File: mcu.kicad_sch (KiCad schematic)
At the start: 28 parts, among them J13 Conn_ARM_JTAG_SWD_10, J3 Conn_01x09_Socket, SW1 SW_SPST, U10 WE-TVS-824015043, U6 STM32F469VETx, Y2 8MHz

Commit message: Some fixes
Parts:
- added C25, C26: .1uF, Capacitor_SMD:C_0805_2012Metric, symbol Device:C
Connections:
- net +3.3V: now also C25.1, C26.1
- net GND: now also C25.2, C26.2
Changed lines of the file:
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@@
 	)
 	(junction
+		(at 139.7 256.54)
+		(diameter 0)
+		(color 0 0 0 0)
+	)
+	(junction
 		(at 185.42 224.79)
 		(diameter 0)
@@
 	)
 	(junction
+		(at 162.56 256.54)
+		(diameter 0)
+		(color 0 0 0 0)
+	)
+	(junction
 		(at 200.66 256.54)
 		(diameter 0)
@@
 	)
 	(junction
+		(at 139.7 224.79)
+		(diameter 0)
+		(color 0 0 0 0)
+	)
+	(junction
 		(at 25.4 72.39)
 		(diameter 0)
@@
 	)
 	(junction
+		(at 162.56 224.79)
+		(diameter 0)
+		(color 0 0 0 0)
+	)
+	(junction
 		(at 215.9 256.54)
 		(diameter 0)
@@
 	(wire
 		(pts
+			(xy 139.7 224.79) (xy 133.35 224.79)
+		)
+		(stroke
+			(width 0)
+			(type default)
+		)
+	)
+	(wire
+		(pts
 			(xy 193.04 234.95) (xy 193.04 224.79)
 		)
@@
 	(wire
 		(pts
+			(xy 162.56 224.79) (xy 170.18 224.79)
+		)
+		(stroke
+			(width 0)
+			(type default)
+		)
+	)
+	(wire
+		(pts
 			(xy 25.4 85.09) (xy 41.91 85.09)
 		)
@@
 	(wire
 		(pts
-			(xy 154.94 224.79) (xy 170.18 224.79)
+			(xy 154.94 224.79) (xy 162.56 224.79)
 		)
 		(stroke
@@
 	(wire
 		(pts
-			(xy 154.94 256.54) (xy 170.18 256.54)
+			(xy 154.94 256.54) (xy 162.56 256.54)
 		)
 		(stroke
@@
 	(wire
 		(pts
+			(xy 133.35 242.57) (xy 133.35 256.54)
+		)
+		(stroke
+			(width 0)
+			(type default)
+		)
+	)
+	(wire
+		(pts
 			(xy 91.44 242.57) (xy 92.71 242.57)
 		)
@@
 	(wire
 		(pts
+			(xy 162.56 256.54) (xy 170.18 256.54)
+		)
+		(stroke
+			(width 0)
+			(type default)
+		)
+	)
+	(wire
+		(pts
 			(xy 50.8 163.83) (xy 60.96 163.83)
 		)
@@
 	(wire
 		(pts
+			(xy 133.35 256.54) (xy 139.7 256.54)
+		)
+		(stroke
+			(width 0)
+			(type default)
+		)
+	)
+	(wire
+		(pts
 			(xy 91.44 232.41) (xy 109.22 232.41)
 		)
@@
 	(wire
 		(pts
+			(xy 162.56 224.79) (xy 162.56 234.95)
+		)
+		(stroke
+			(width 0)
+			(type default)
+		)
+	)
+	(wire
+		(pts
 			(xy 223.52 242.57) (xy 223.52 256.54)
 		)
@@
 	(wire
 		(pts
+			(xy 162.56 242.57) (xy 162.56 256.54)
+		)
+		(stroke
+			(width 0)
+			(type default)
+		)
+	)
+	(wire
+		(pts
 			(xy 25.4 67.31) (xy 41.91 67.31)
 		)
@@
 	(wire
 		(pts
+			(xy 133.35 224.79) (xy 133.35 234.95)
+		)
+		(stroke
+			(width 0)
+			(type default)
+		)
+	)
+	(wire
+		(pts
 			(xy 177.8 224.79) (xy 185.42 224.79)
 		)
@@
 	(symbol
 		(lib_id "Device:C")
+		(at 133.35 238.76 0)
+		(unit 1)
+		(exclude_from_sim no)
+		(in_bom yes)
+		(on_board yes)
+		(dnp no)
+		(property "Reference" "C26"
+			(at 135.382 235.966 0)
+			(effects
+				(font
+					(size 1.27 1.27)
+				)
+				(justify left)
+			)
+		)
+		(property "Value" ".1uF"
+			(at 135.382 241.554 0)
+			(effects
+				(font
+					(size 1.27 1.27)
+				)
+				(justify left)
+			)
+		)
+		(property "Footprint" "Capacitor_SMD:C_0805_2012Metric"
+			(at 134.3152 242.57 0)
+			(effects
+				(font
+					(size 1.27 1.27)
+				)
+				(hide yes)
+			)
+		)
+		(property "Datasheet" "~"
+			(at 133.35 238.76 0)
+			(effects
+				(font
+					(size 1.27 1.27)
+				)
+				(hide yes)
+			)
+		)
+		(property "Description" "Unpolarized capacitor"
+			(at 133.35 238.76 0)
+			(effects
+				(font
+					(size 1.27 1.27)
+				)
+				(hide yes)
+			)
+		)
+		(pin "2"
+		)
+		(pin "1"
+		)
+		(instances
+			(project "senior_design"
+				(path "/35c074f0-8545-4dc1-a57d-3ef0bc7d9188/332aa9c6-46d1-4f07-ac6a-0c48b9b46fa2"
+					(reference "C26")
+					(unit 1)
+				)
+			)
+		)
+	)
+	(symbol
+		(lib_id "Device:C")
 		(at 215.9 238.76 0)
 		(unit 1)
@@
 					(unit 1)
 				)
+			)
+		)
+	)
+	(symbol
+		(lib_id "Device:C")
+		(at 162.56 238.76 0)
+		(unit 1)
+		(exclude_from_sim no)
+		(in_bom yes)
+		(on_board yes)
+		(dnp no)
+		(property "Reference" "C25"
+			(at 164.592 235.966 0)
+			(effects
+				(font
+					(size 1.27 1.27)
+				)
+				(justify left)
+			)
+		)
+		(property "Value" ".1uF"
+			(at 164.592 241.554 0)
+			(effects
+				(font
+					(size 1.27 1.27)
+				)
+				(justify left)
+			)
+		)
+		(property "Footprint" "Capacitor_SMD:C_0805_2012Metric"
+			(at 163.5252 242.57 0)
+			(effects
+				(font
+					(size 1.27 1.27)
+				)
+				(hide yes)
+			)
+		)
+		(property "Datasheet" "~"
+			(at 162.56 238.76 0)
+			(effects
+				(font
+					(size 1.27 1.27)
+				)
+				(hide yes)
+			)
+		)
+		(property "Description" "Unpolarized capacitor"
+			(at 162.56 238.76 0)
+			(effects
+				(font
+					(size 1.27 1.27)
+				)
+				(hide yes)
+			)
+		)
+		(pin "2"
+		)
+		(pin "1"
+		)
+		(instances
+			(project "senior_design"
+				(path "/35c074f0-8545-4dc1-a57d-3ef0bc7d9188/332aa9c6-46d1-4f07-ac6a-0c48b9b46fa2"
+					(reference "C25")
+					(unit 1)
+				)

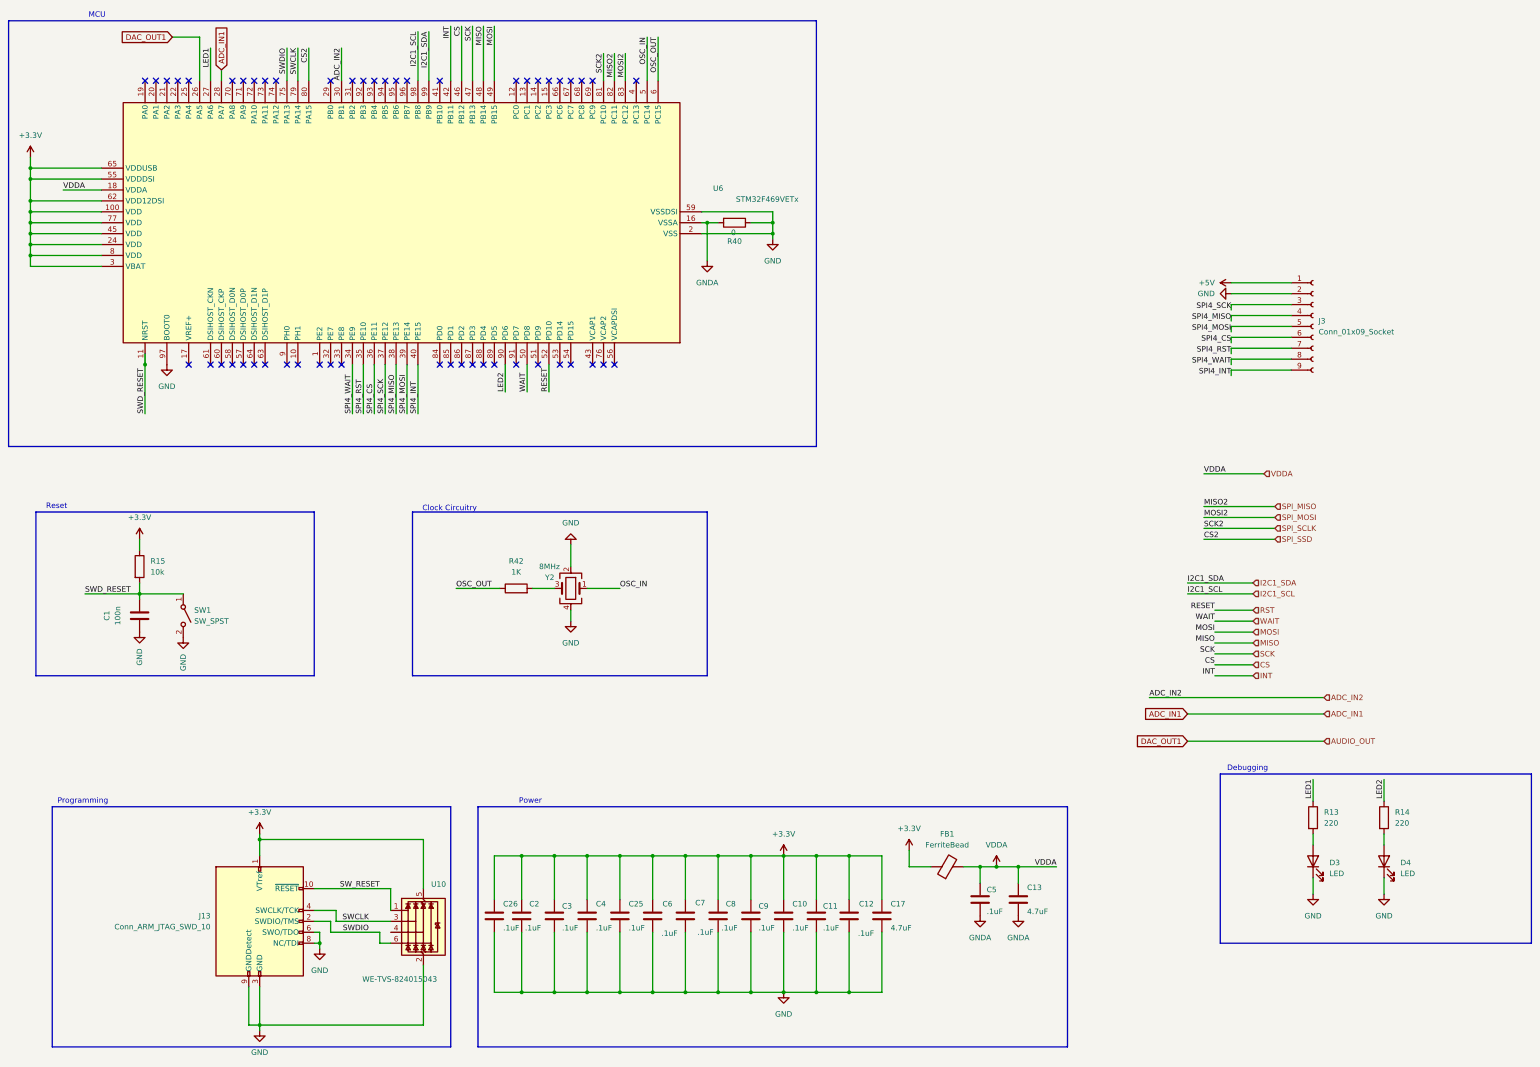
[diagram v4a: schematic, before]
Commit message: Fixed labels and added datasheets
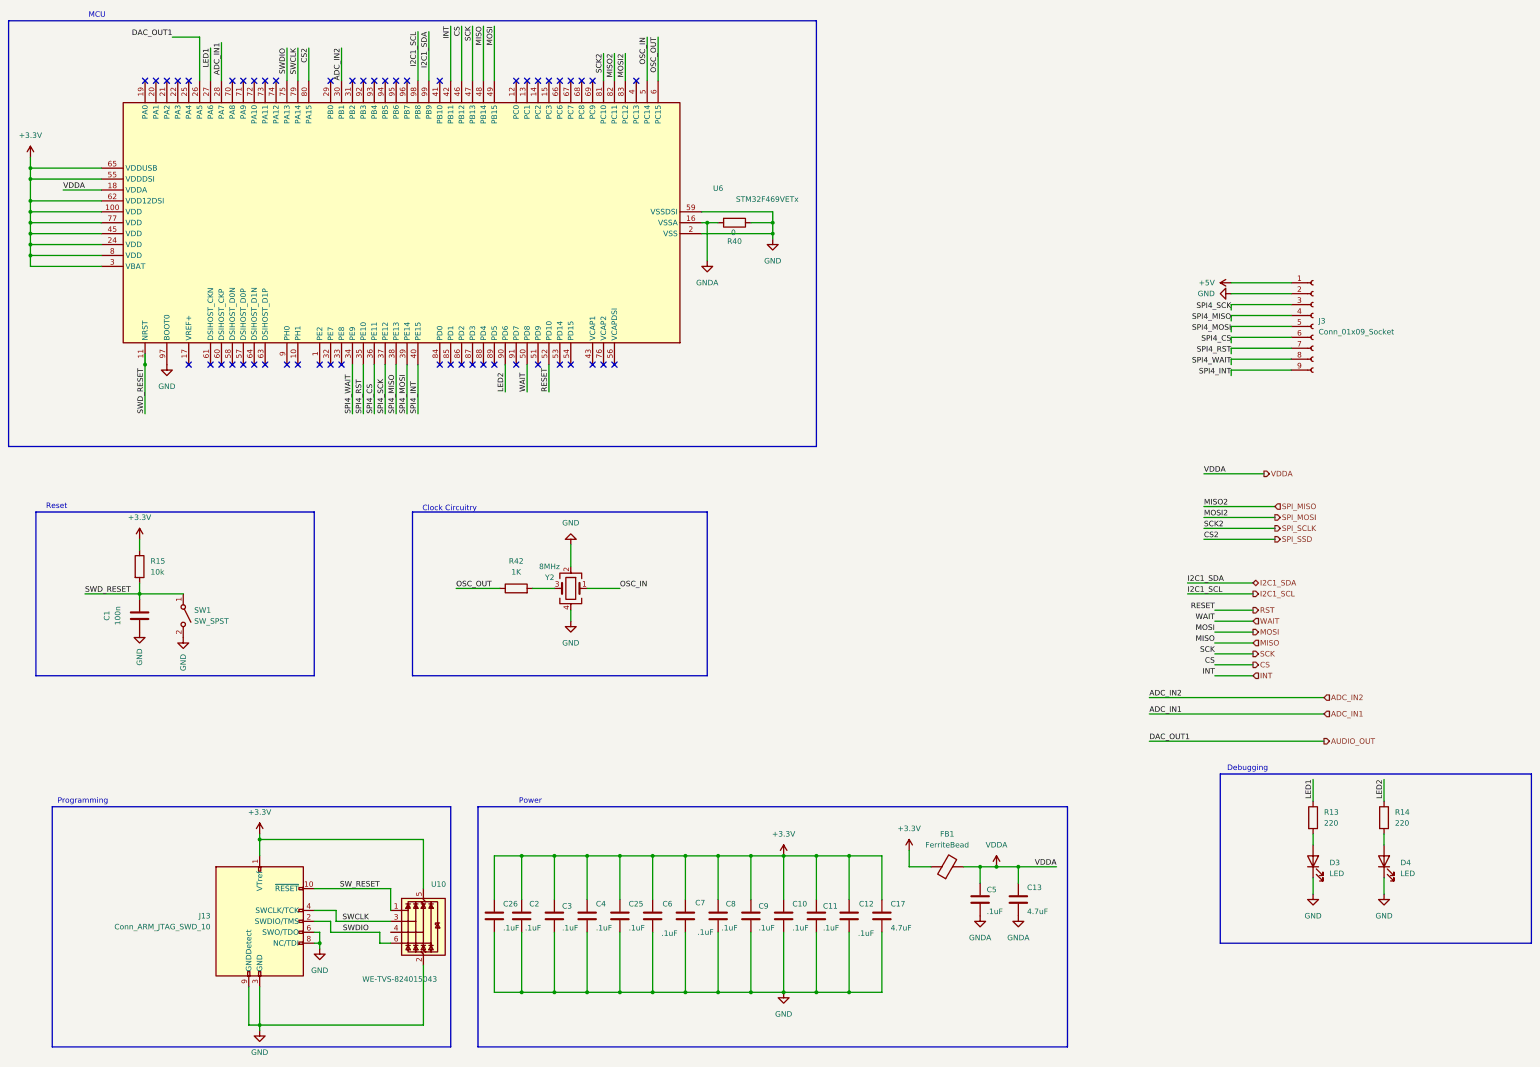
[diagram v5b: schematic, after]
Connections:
- net DAC_OUT1 renamed AUDIO_OUT
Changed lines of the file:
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@@
+	(wire
+		(pts
+			(xy 69.85 35.56) (xy 69.85 44.45)
+		)
+		(stroke
+			(width 0)
+			(type default)
+		)
+	)
 	(wire
 		(pts
@@
 	(wire
 		(pts
-			(xy 69.85 41.91) (xy 69.85 44.45)
-		)
-		(stroke
-			(width 0)
-			(type default)
-		)
-	)
-	(wire
-		(pts
 			(xy 300.99 167.64) (xy 309.88 167.64)
 		)
@@
 	(wire
 		(pts
+			(xy 285.75 198.12) (xy 326.39 198.12)
+		)
+		(stroke
+			(width 0)
+			(type default)
+		)
+	)
+	(wire
+		(pts
 			(xy 25.4 64.77) (xy 25.4 62.23)
 		)
@@
 	(wire
 		(pts
-			(xy 294.64 191.77) (xy 326.39 191.77)
-		)
-		(stroke
-			(width 0)
-			(type default)
-		)
-	)
-	(wire
-		(pts
 			(xy 171.45 34.29) (xy 171.45 44.45)
 		)
@@
 	(wire
 		(pts
-			(xy 294.64 198.12) (xy 326.39 198.12)
-		)
-		(stroke
-			(width 0)
-			(type default)
-		)
-	)
-	(wire
-		(pts
 			(xy 25.4 82.55) (xy 25.4 80.01)
 		)
@@
 		(pts
 			(xy 50.8 163.83) (xy 50.8 165.1)
+		)
+		(stroke
+			(width 0)
+			(type default)
+		)
+	)
+	(wire
+		(pts
+			(xy 285.75 191.77) (xy 326.39 191.77)
 		)
 		(stroke
@@
 		)
 	)
+	(label "ADC_IN1"
+		(at 285.75 191.77 0)
+		(effects
+			(font
+				(size 1.27 1.27)
+			)
+			(justify left bottom)
+		)
+	)
 	(label "SCK2"
 		(at 298.45 148.59 0)
@@
 		)
 	)
+	(label "ADC_IN1"
+		(at 69.85 35.56 270)
+		(effects
+			(font
+				(size 1.27 1.27)
+			)
+			(justify right bottom)
+		)
+	)
 	(label "SPI4_INT"
 		(at 304.8 113.03 180)
@@
 		)
 	)
+	(label "DAC_OUT1"
+		(at 285.75 198.12 0)
+		(effects
+			(font
+				(size 1.27 1.27)
+			)
+			(justify left bottom)
+		)
+	)
 	(label "SPI4_MISO"
 		(at 110.49 121.92 90)
@@
 		)
 	)
+	(label "DAC_OUT1"
+		(at 58.42 34.29 180)
+		(effects
+			(font
+				(size 1.27 1.27)
+			)
+			(justify right bottom)
+		)
+	)
 	(label "SPI4_MISO"
 		(at 304.8 100.33 180)
@@
 			)
 			(justify right bottom)
-		)
-	)
-	(global_label "ADC_IN1"
-		(shape input)
-		(at 294.64 191.77 180)
-		(fields_autoplaced yes)
-		(effects
-			(font
-				(size 1.27 1.27)
-			)
-			(justify right)
-		)
-		(property "Intersheetrefs" "${INTERSHEET_REFS}"
-			(at 283.9138 191.77 0)
-			(effects
-				(font
-					(size 1.27 1.27)
-				)
-				(justify right)
-				(hide yes)
-			)
-		)
-	)
-	(global_label "DAC_OUT1"
-		(shape input)
-		(at 58.42 34.29 180)
-		(fields_autoplaced yes)
-		(effects
-			(font
-				(size 1.27 1.27)
-			)
-			(justify right)
-		)
-		(property "Intersheetrefs" "${INTERSHEET_REFS}"
-			(at 46.0005 34.29 0)
-			(effects
-				(font
-					(size 1.27 1.27)
-				)
-				(justify right)
-				(hide yes)
-			)
-		)
-	)
-	(global_label "DAC_OUT1"
-		(shape input)
-		(at 294.64 198.12 180)
-		(fields_autoplaced yes)
-		(effects
-			(font
-				(size 1.27 1.27)
-			)
-			(justify right)
-		)
-		(property "Intersheetrefs" "${INTERSHEET_REFS}"
-			(at 282.2205 198.12 0)
-			(effects
-				(font
-					(size 1.27 1.27)
-				)
-				(justify right)
-				(hide yes)
-			)
-		)
-	)
-	(global_label "ADC_IN1"
-		(shape input)
-		(at 69.85 41.91 90)
-		(fields_autoplaced yes)
-		(effects
-			(font
-				(size 1.27 1.27)
-			)
-			(justify left)
-		)
-		(property "Intersheetrefs" "${INTERSHEET_REFS}"
-			(at 69.85 31.1838 90)
-			(effects
-				(font
-					(size 1.27 1.27)
-				)
-				(justify left)
-				(hide yes)
-			)
 		)
 	)
@@
 	)
 	(hierarchical_label "MOSI"
-		(shape input)
+		(shape output)
 		(at 309.88 172.72 0)
 		(effects
@@
 	)
 	(hierarchical_label "I2C1_SCL"
-		(shape input)
+		(shape output)
 		(at 309.88 163.83 0)
 		(effects
@@
 	)
 	(hierarchical_label "RST"
-		(shape input)
+		(shape output)
 		(at 309.88 167.64 0)
 		(effects
@@
 	)
 	(hierarchical_label "SPI_SCLK"
-		(shape input)
+		(shape output)
 		(at 314.96 148.59 0)
 		(effects
@@
 	)
 	(hierarchical_label "AUDIO_OUT"
-		(shape input)
+		(shape output)
 		(at 326.39 198.12 0)
 		(effects
@@
 	)
 	(hierarchical_label "VDDA"
-		(shape input)
+		(shape output)
 		(at 312.42 135.89 0)
 		(effects
@@
 	)
 	(hierarchical_label "SCK"
-		(shape input)
+		(shape output)
 		(at 309.88 177.8 0)
 		(effects
@@
 	)
 	(hierarchical_label "I2C1_SDA"
-		(shape input)
+		(shape bidirectional)
 		(at 309.88 161.29 0)
 		(effects
@@
 	)
 	(hierarchical_label "SPI_MOSI"
-		(shape input)
+		(shape output)
 		(at 314.96 146.05 0)
 		(effects
@@
 	)
 	(hierarchical_label "SPI_SSD"
-		(shape input)
+		(shape output)
 		(at 314.96 151.13 0)
 		(effects
@@
 	)
 	(hierarchical_label "CS"
-		(shape input)
+		(shape output)
 		(at 309.88 180.34 0)
 		(effects

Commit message: changed spis
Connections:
- net SPI4_INT: now also U6.74 (PA12); no longer U6.40 (PE15)
- net SPI4_RST: now also U6.73 (PA11); no longer U6.35 (PE10)
- net SPI4_WAIT: now also U6.72 (PA10); no longer U6.34 (PE9)
- net SPI_MISO: now also U6.37 (PE12); no longer U6.82 (PC11)
- net SPI_MOSI: now also U6.38 (PE13); no longer U6.83 (PC12)
- net SPI_SCLK: now also U6.39 (PE14); no longer U6.81 (PC10)
- net SPI_SSD: now also U6.36 (PE11); no longer U6.80 (PA15)
- net SPI4_CS renamed MISO2
- net MISO2: now also U6.82 (PC11); no longer U6.36 (PE11)
- net SPI4_MISO renamed SCK2
- net SCK2: now also U6.81 (PC10); no longer U6.38 (PE13)
- net SPI4_MOSI renamed MOSI2
- net MOSI2: now also U6.83 (PC12); no longer U6.39 (PE14)
- net SPI4_SCK renamed CS2
- net CS2: now also U6.80 (PA15); no longer U6.37 (PE12)

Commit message: fixed some of the problems
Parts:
- added C27, C35: 10pF, Capacitor_SMD:C_0402_1005Metric, symbol Device:C
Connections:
- net GND: now also C27.2, C35.2
- net OSC_IN: now also C27.1
- net at R42.2, Y2.3: now also C35.1
